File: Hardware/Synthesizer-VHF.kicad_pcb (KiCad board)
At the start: 2 copper layers, 45.8 x 32.5 mm, 81 parts, among them J1 REF Select, J2 REF_IN, J3 RFOUTA, J4 RFOUTB, J5 USB-C 2.0 16P, J7 Header 1x3, J8 Screw_Terminal_01x12, U10 ADF4350, U2 MC78L05_TO-252, U4 GM1207ACPZ-3.3, U7 GM1207ACPZ-3.3, U8 ATtiny1616-M, U9 FT231XQ, X1 IQXO-70

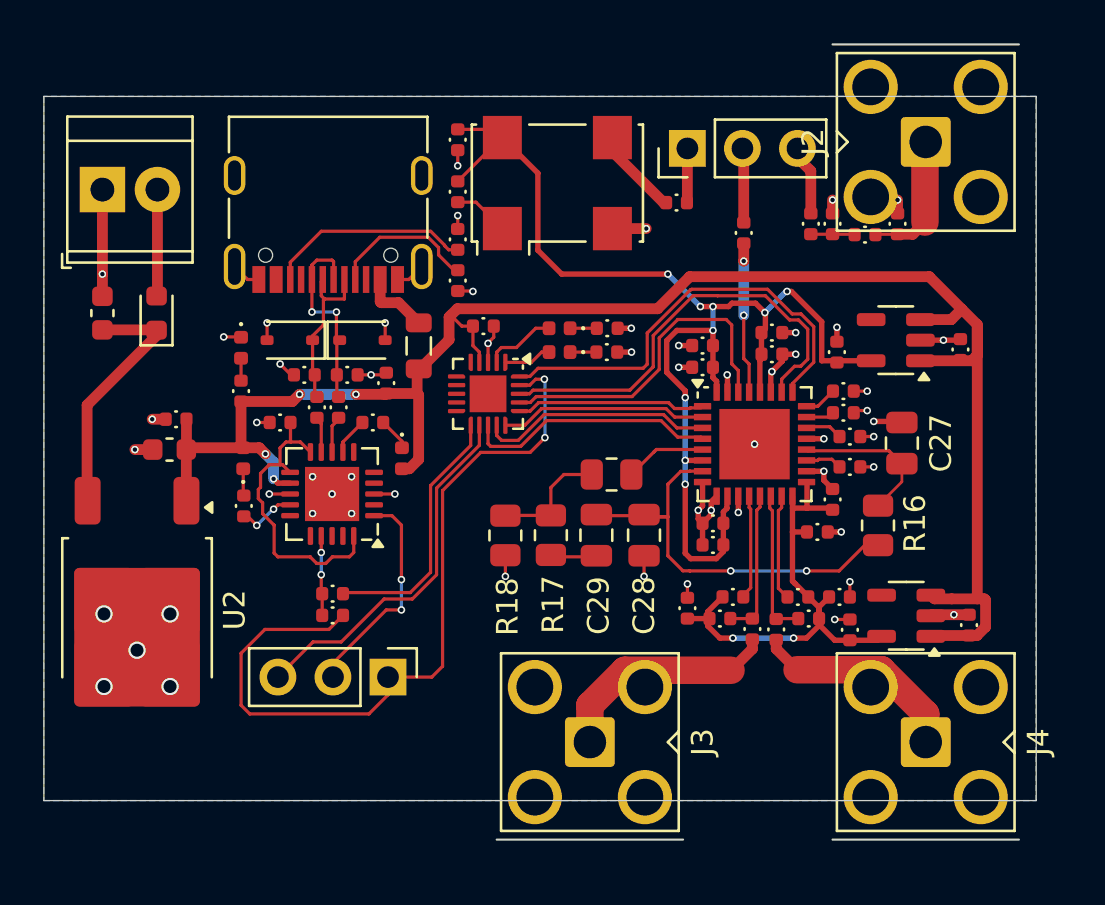
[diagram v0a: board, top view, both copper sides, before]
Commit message: Added test points for scope probes, tweaked layout a bit
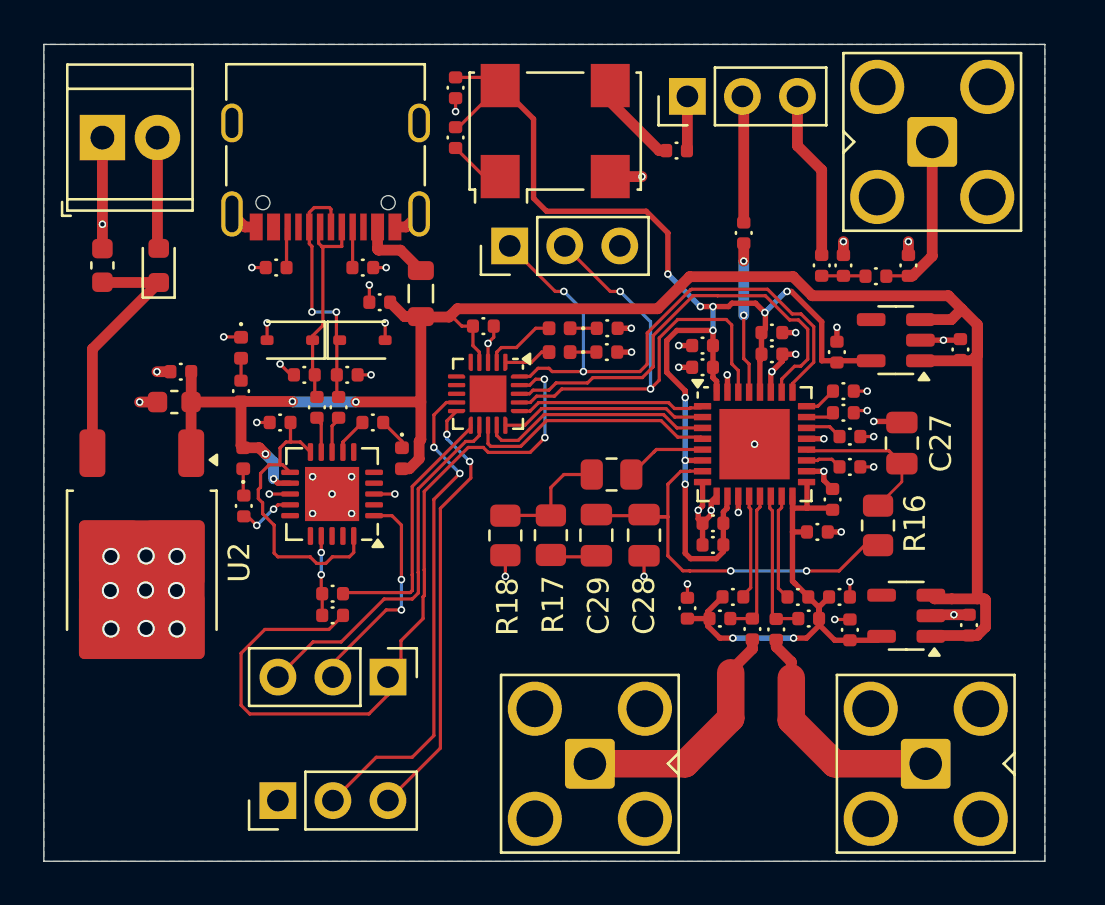
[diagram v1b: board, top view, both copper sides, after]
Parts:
- added J6: Header 1x3, Connector_PinHeader_2.54mm:PinHeader_1x03_P2.54mm_Vertical, F.Cu at (148.8, 85.3)
- added J9: Header 1x3, Connector_PinHeader_2.54mm:PinHeader_1x03_P2.54mm_Vertical, F.Cu at (138.1, 110.9)
- D5: value White -> PA2
- D8: value White -> PA3
- J2, J3, J4: footprint Connector_Coaxial:SMA_Amphenol_901-143_Horizontal -> Synthesizer:SMA_Amphenol_901-143_Horizontal
- moved R10 8.48 mm to (138.0, 86.3), turned to 0 degrees
- moved R7 4.42 mm to (142.0, 86.3), turned to 180 degrees
- moved C44 3.74 mm to (142.8, 87.9), turned to 180 degrees
- moved R21 2.50 mm to (146.3, 80.3)
- moved J5 2.43 mm to (140.3, 80.7)
- moved FB1 2.41 mm to (144.7, 87.5)
- moved C31 2.40 mm to (146.3, 78.0)
- moved X1 2.40 mm to (150.9, 80.0)
- moved J8 2.40 mm to (130.0, 80.3)
- moved J1 2.40 mm to (157.0, 78.4)
- moved R20 2.40 mm to (156.5, 80.9)
- moved C47 2.21 mm to (133.6, 91.1)
- moved C48 2.21 mm to (133.3, 92.5)
- moved U2 2.21 mm to (131.8, 99.9)
- moved D1 2.20 mm to (132.6, 86.2)
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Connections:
- U8 pad 10: unconnected-(U8-PB4-Pad10) -> Net-(J9-Pin_3)
- U8 pad 9: unconnected-(U8-PB5-Pad9) -> Net-(J9-Pin_2)
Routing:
- net Net-(J9-Pin_2): track 0.00 -> 23.0 mm, vias 0 -> 2
- net Net-(J9-Pin_3): track 0.00 -> 20.2 mm, vias 0 -> 2
- net /MUX: track 15.6 -> 24.4 mm, vias 0 -> 2
- net Net-(J5-CC2): track 9.49 -> 1.90 mm
- net /LD: track 20.3 -> 27.9 mm, vias 0 -> 2
- net Net-(J5-CC1): track 6.85 -> 1.88 mm
- net Net-(J1-Pin_3): track 3.25 -> 7.78 mm
- net /VCC_DIG: track 56.0 -> 59.2 mm
- net Net-(D2-K): track 9.39 -> 11.9 mm
- net Net-(D4-K): track 7.69 -> 10.1 mm
- net Net-(J1-Pin_2): track 3.45 -> 5.85 mm
- net /5V: track 82.3 -> 84.5 mm
- net Net-(J2-In): track 6.24 -> 7.77 mm
- net Net-(J4-In): track 9.86 -> 11.0 mm
- net Net-(J3-In): track 10.7 -> 11.4 mm
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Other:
- board size 45.8 x 32.5 mm -> 46.2 x 37.7 mm

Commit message: Tried to find a better TCXO at 40 MHz, but jlcpcb froze all of kicad several times.
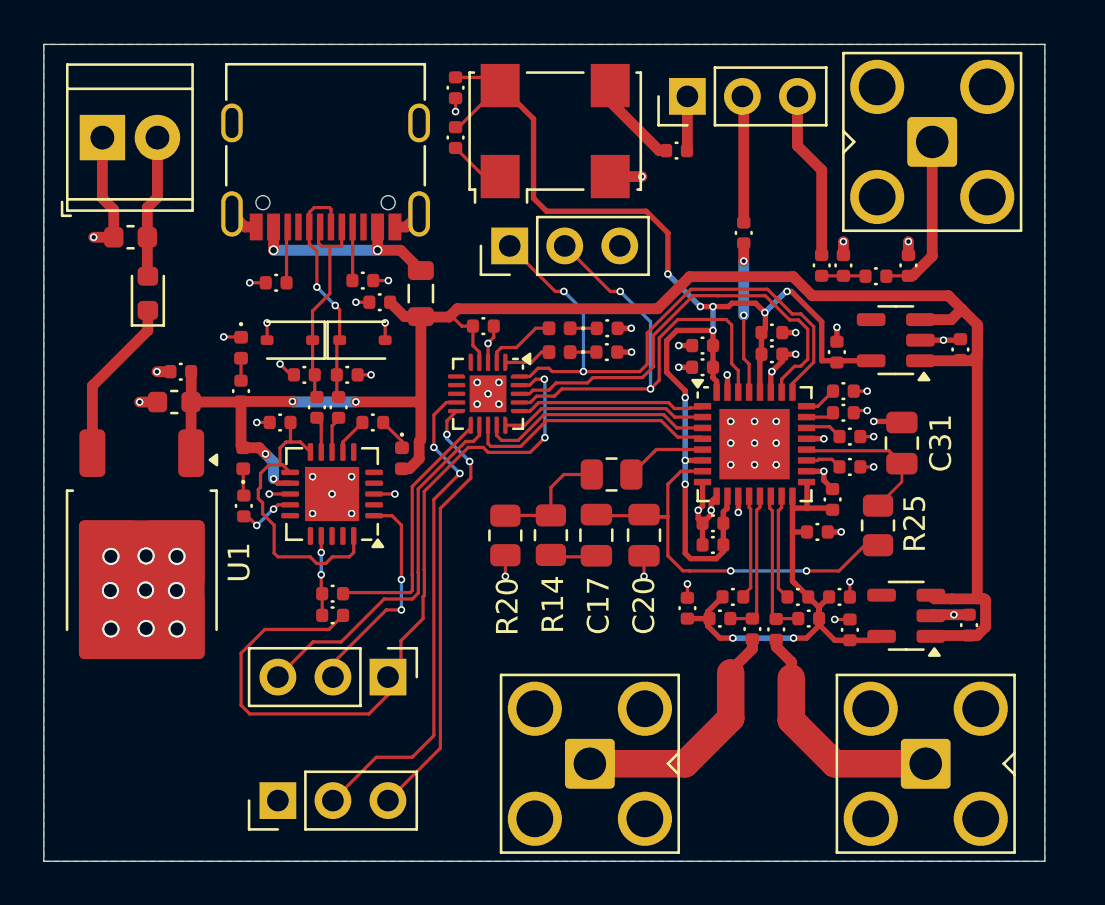
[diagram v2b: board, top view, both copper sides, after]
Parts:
- moved C1 1.84 mm to (131.3, 84.9), turned to 180 degrees
- moved D1 1.38 mm to (132.1, 87.5)
- moved R1 0.70 mm to (138.0, 87.0)
- moved R3 0.60 mm to (142.0, 86.9)
- renumbered C26 to C1, C5 to C10, C45 to C11, C6 to C12, C11 to C13, C34 to C14, C1 to C15, C2 to C16, C29 to C17, C9 to C18, C12 to C19, C44 to C2, C28 to C20, C8 to C21, C24 to C22, C22 to C23, C16 to C24, C15 to C25, C4 to C26, C41 to C27, C10 to C28, C42 to C29, C7 to C30, C27 to C31, C40 to C32, C35 to C33, C13 to C4, C31 to C5, C47 to C6, C46 to C7, C48 to C8, C43 to C9, D4 to D2, D6 to D4, D7 to D5, D2 to D6, D5 to D7, J8 to J1, J6 to J2, J1 to J3, J5 to J4, J2 to J5, J9 to J6, J3 to J7, J7 to J8, J4 to J9, R10 to R1, R26 to R10, R6 to R11, R30 to R12, R25 to R13, R17 to R14, R5 to R15, R29 to R16, R12 to R17, R8 to R18, R28 to R19, R20 to R2, R18 to R20, R3 to R21, R4 to R22, R2 to R23, R16 to R25, R7 to R3, R21 to R4, R9 to R5, R19 to R6, R1 to R7, R27 to R8, R11 to R9, U2 to U1, U9 to U2, U8 to U3, U10 to U4, U7 to U5, U4 to U6
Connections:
- C1 pad 1: Net-(D1-K) -> /12V
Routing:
- net Net-(FB1-Pad1): track 3.43 -> 9.34 mm, vias 0 -> 2
- net Net-(D1-K): track 11.8 -> 7.69 mm
- net /12V: track 5.14 -> 6.60 mm
- net Net-(J5-CC2): track 1.90 -> 2.60 mm
- net Net-(D2-K): track 11.9 -> 11.2 mm
- net GND: track 50.0 -> 50.7 mm, vias 61 -> 74
- net Net-(J5-CC1): track 1.88 -> 2.48 mm

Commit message: Complete design used for pricing experient.   0.2 mm drilled vias cost a lot.   had assembling through hole adds a lot   4 layers is is free Next up,   climb the learning curve on 4 layer design   price components on both sides
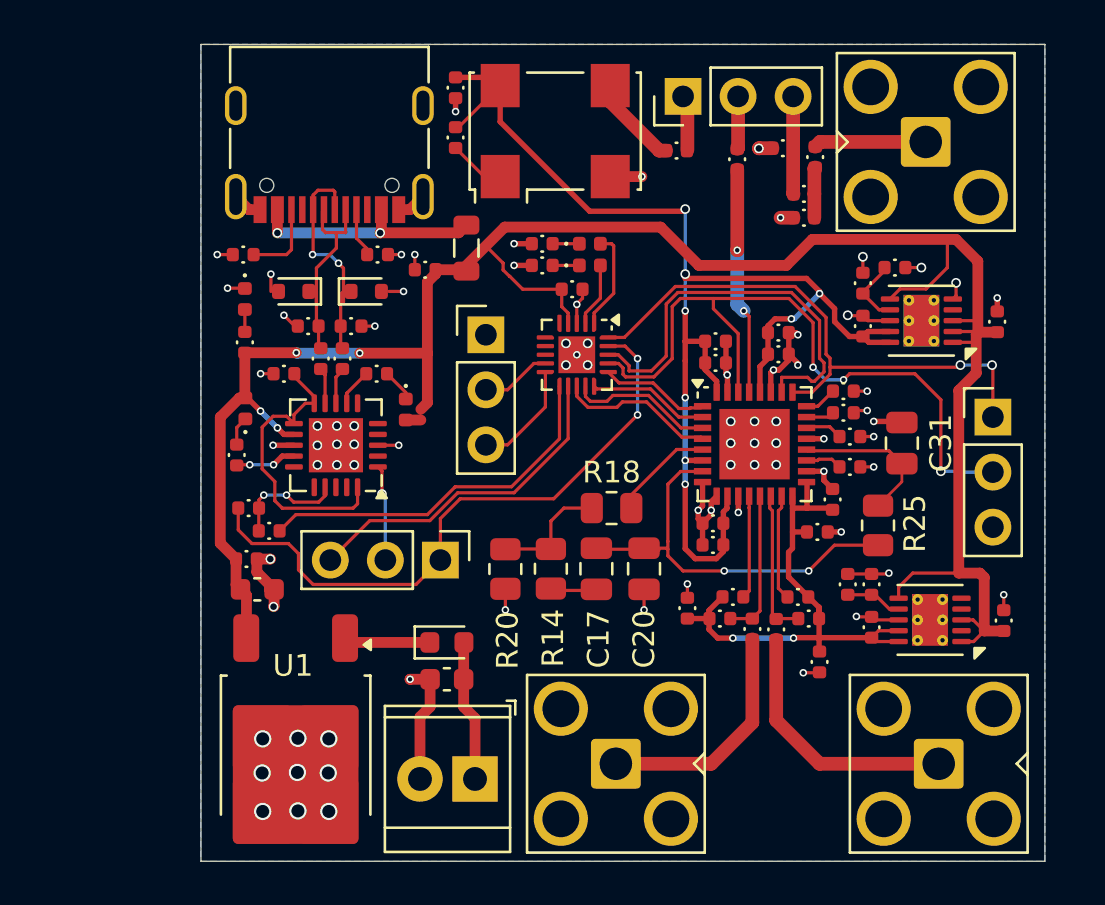
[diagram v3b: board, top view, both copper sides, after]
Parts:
- added C34: 4.7u 10V, Synthesizer:Cap_0402, F.Cu at (165.1, 87.0)
- added C35: 4.7u 10V, Synthesizer:Cap_0402, F.Cu at (165.5, 100.9)
- added R26: 33K2, Synthesizer:Res_0402, F.Cu at (164.4, 100.9)
- added R27: 33K2, Synthesizer:Res_0402, F.Cu at (166.6, 86.3)
- C1: value 330n 25V -> 330n 50V
- C14, C27, C32, C33: value 2.2u -> 4.7u 10V
- C2, C29, C6, C7: value .1u -> 100n
- C31: value 680 -> 680p
- D2, D6: footprint Diode_SMD:D_SOD-323 -> Diode_SMD:D_SOD-523
- J1: value Screw_Terminal_01x12 -> Screw_Terminal_01x02
- J2, J6: value Header 1x3 -> Scope
- R13, R24: value 22 -> 22R
- R2: value 0 -> 0R
- U1: value MC78L05_TO-252 -> LM7805A
- U5, U6: value GM1207ACPZ-3.3 -> GM1200ACPZ; footprint Package_TO_SOT_SMD:SOT-23-5 -> Package_DFN_QFN:DFN-10-1EP_3x3mm_P0.5mm_EP1.65x2.38mm_ThermalVias
- moved J1 34.2 mm to (147.2, 109.9), turned to 180 degrees
- moved C1 25.1 mm to (145.9, 105.3)
- moved J2 23.7 mm to (171.1, 93.2), turned to 0 degrees
- moved J6 23.5 mm to (147.7, 89.4), turned to 0 degrees
- moved D1 21.2 mm to (145.9, 103.6), turned to 0 degrees
- moved U1 11.1 mm to (138.9, 108.4)
- moved C8 9.45 mm to (137.2, 101.2), turned to 0 degrees
- moved C6 9.16 mm to (136.7, 99.8), turned to 0 degrees
- moved R6 7.93 mm to (161.4, 80.8), turned to 180 degrees
- moved R12 6.29 mm to (136.8, 97.4), turned to 180 degrees
- moved J8 5.92 mm to (145.6, 99.8)
- moved R10 5.82 mm to (150.3, 85.2), turned to 180 degrees
- moved D7 5.19 mm to (152.5, 85.2), turned to 0 degrees
- moved R7 5.05 mm to (162.4, 82.9)
- moved C4 5.01 mm to (162.9, 81.2), turned to 90 degrees
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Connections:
- C4 pad 1: Net-(J1-Pin_3) -> Net-(C4-Pad1)
- C4 pad 2: Net-(C13-Pad2) -> Net-(J5-In)
- J1 pad 1: GND -> /12V
- J1 pad 2: /12V -> GND
- J3 pad 3: Net-(J1-Pin_3) -> Net-(J3-Pin_3)
- J5 pad 1: Net-(J2-In) -> Net-(J5-In)
- R5 pad 1: Net-(C13-Pad2) -> Net-(C4-Pad1)
- R6 pad 1: Net-(J2-In) -> Net-(J3-Pin_3)
- R7 pad 1: Net-(J2-In) -> Net-(C4-Pad1)
- R7 pad 2: Net-(C13-Pad2) -> Net-(J3-Pin_3)
- U1 pad 1: /5V -> Net-(D1-K)
- U1 pad 3: Net-(D1-K) -> /5V
- U2 pad 19: /RTS\ -> unconnected-(U2-~{RTS}-Pad19)
- U2 pad 6: /CTS\ -> unconnected-(U2-~{CTS}-Pad6)
- U5 pad 2: GND -> /5V
- U5 pad 5: /VCC_DIG -> GND
- U6 pad 2: GND -> /5V
- U6 pad 5: /VCC_RF -> GND
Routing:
- net Net-(J6-Pin_2): track 23.0 -> 3.25 mm, vias 2 -> 0
- net /5V: track 84.5 -> 100.9 mm
- net Net-(J6-Pin_3): track 20.2 -> 5.08 mm, vias 2 -> 0
- net /MUX: track 24.4 -> 32.6 mm, vias 2 -> 3
- net GND: track 50.7 -> 58.8 mm, vias 74 -> 80
- net Net-(J1-Pin_3): track 7.78 -> 0.00 mm
- net Net-(J2-In): track 7.77 -> 0.00 mm
- net /UPDI: track 35.9 -> 29.5 mm
- net /RXD_U: track 10.2 -> 4.44 mm, vias 2 -> 1
- net Net-(J5-In): track 0.00 -> 5.49 mm
- net /RXD_M: track 12.0 -> 17.1 mm
- net Net-(J3-Pin_3): track 0.00 -> 4.51 mm
- net /CE: track 11.6 -> 7.29 mm
- net /LE: track 10.8 -> 6.71 mm
- net /DATA: track 9.58 -> 5.60 mm
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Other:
- board size 46.2 x 37.7 mm -> 38.9 x 37.7 mm

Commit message: Updated layout for 4 layer board as an experiment to check costs Changed low noise regulators to ADP150...used in the Eval board and fancy sig gen example Add more analysis to phase noise spreadsheet, apparently the low V/Hz of the VCO allows cheap regulators
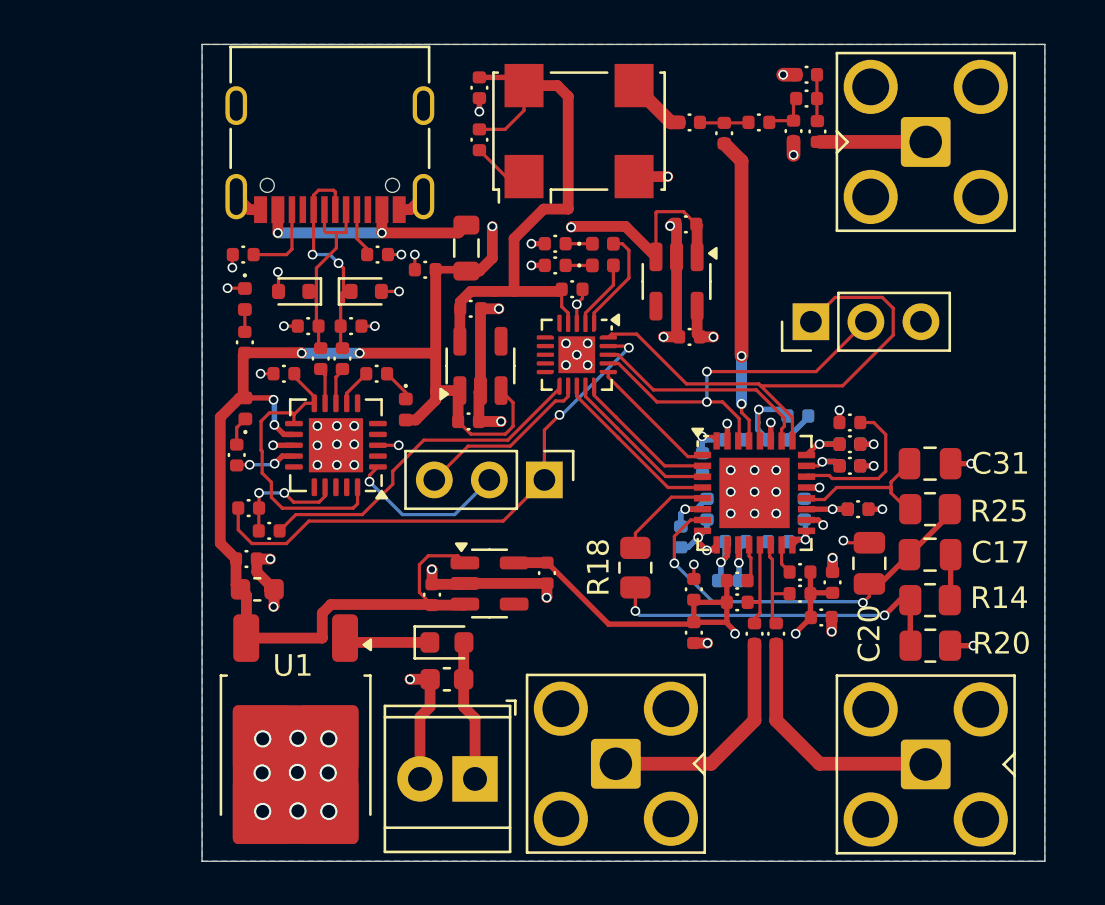
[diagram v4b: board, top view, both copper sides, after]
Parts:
- removed C34, C35: 4.7u 10V, Synthesizer:Cap_0402
- removed J3: REF Select, Connector_PinHeader_2.54mm:PinHeader_1x03_P2.54mm_Vertical
- removed J6: Scope, Connector_PinHeader_2.54mm:PinHeader_1x03_P2.54mm_Vertical
- removed R26, R27: 33K2, Synthesizer:Res_0402
- added C36: 10p, Synthesizer:Cap_0402, B.Cu at (164.5, 94.5)
- added C37: 10p, Synthesizer:Cap_0402, B.Cu at (164.5, 95.5)
- added C38: 10p, Synthesizer:Cap_0402, B.Cu at (164.9, 97.4)
- added C39: 100n, Synthesizer:Cap_0402, B.Cu at (158.9, 100.8)
- added C40: 10p, Synthesizer:Cap_0402, B.Cu at (159.2, 98.9)
- added C41: 100n, Synthesizer:Cap_0402, F.Cu at (157.3, 103.2)
- added C42: 100n, Synthesizer:Cap_0402, F.Cu at (163.2, 102.4)
- added C43: 120p, Synthesizer:Cap_0402, F.Cu at (163.7, 100.8)
- added C44: 1u, Synthesizer:Cap_0402, F.Cu at (146.9, 93.4)
- added R28: NP, Synthesizer:Res_0402, F.Cu at (160.3, 79.6)
- added U7: ADP150AUJZ-3.3-R7, Package_TO_SOT_SMD:SOT-23-5, F.Cu at (147.4, 90.8)
- C13, C18, C25, C30: value 10n -> 100n; moved to B.Cu
- C14, C27, C32, C33: value 4.7u 10V -> 1u
- C15: value 100n -> 120p
- C19, C21, C24, C28: value 100p -> 10p; moved to B.Cu
- C22: value 100n -> 1u
- C3: value 10n -> 1n
- U4: value ADF4350 -> ADF435x
- U5, U6: value GM1200ACPZ -> ADP150AUJZ-3.3-R7; footprint Package_DFN_QFN:DFN-10-1EP_3x3mm_P0.5mm_EP1.65x2.38mm_ThermalVias -> Package_TO_SOT_SMD:SOT-23-5
- moved C22 22.9 mm to (147.0, 88.2), turned to 0 degrees
- moved C33 21.2 mm to (150.5, 100.4), turned to -90 degrees
- moved U6 20.4 mm to (147.9, 100.9), turned to 0 degrees
- moved C14 20.3 mm to (145.2, 101.4)
- moved R20 19.9 mm to (168.2, 103.8), turned to 0 degrees
- moved R14 17.6 mm to (168.2, 101.7), turned to 180 degrees
- moved C17 15.4 mm to (168.2, 99.5), turned to 0 degrees
- moved C32 14.2 mm to (157.1, 89.5), turned to 180 degrees
- moved U5 11.4 mm to (156.5, 86.9), turned to -90 degrees
- moved C20 10.4 mm to (165.4, 100.0), turned to 90 degrees
- moved J2 9.48 mm to (162.7, 88.8), turned to 90 degrees
- moved C27 9.42 mm to (156.9, 84.3), turned to 180 degrees
- moved R5 6.60 mm to (162.5, 77.4)
- moved J8 6.06 mm to (150.4, 96.1)
- moved C13 5.68 mm to (157.7, 95.3), turned to -90 degrees
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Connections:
- C13 pad 1: /VCC_DIG -> /VCC_1
- C14 pad 1: /VCC_RF -> /5V
- C15 pad 1: /VCC_RF -> /VCC_2
- C18 pad 1: /VCC_RF -> /VCC_1
- C19 pad 2: /VCC_DIG -> /VCC_1
- C21 pad 2: /VCC_DIG -> /VCC_1
- C22 pad 1: /VCC_RF -> /3V3_MCU
- C24 pad 1: /VCC_DIG -> /VCC_1
- C25 pad 1: /VCC_DIG -> /VCC_1
- C27 pad 1: /VCC_DIG -> /5V
- C28 pad 2: /VCC_RF -> /VCC_1
- C29 pad 1: /5V -> /3V3_MCU
- C3 pad 2: Net-(J3-Pin_2) -> Net-(C3-Pad2)
- C30 pad 1: /VCC_DIG -> /VCC_1
- C32 pad 1: /5V -> /VCC_1
- C33 pad 1: /5V -> /VCC_2
- C5 pad 2: /VCC_DIG -> /3V3_MCU
- R11 pad 2: /VCC_RF -> /VCC_2
- R15 pad 2: /VCC_RF -> /VCC_2
- R2 pad 1: Net-(X1-OUT) -> Net-(C3-Pad2)
- R2 pad 2: Net-(J3-Pin_1) -> Net-(X1-OUT)
- R21 pad 2: /VCC_RF -> /VCC_2
- R23 pad 2: /VCC_RF -> /VCC_2
- R4 pad 2: /VCC_DIG -> /3V3_MCU
- U3 pad 10: Net-(J6-Pin_3) -> unconnected-(U3-PB4-Pad10)
- U3 pad 4: /5V -> /3V3_MCU
- U3 pad 9: Net-(J6-Pin_2) -> unconnected-(U3-PB5-Pad9)
- U4 pad 10: /VCC_DIG -> /VCC_1
- U4 pad 16: /VCC_RF -> /VCC_1
- U4 pad 17: /VCC_RF -> /VCC_1
- U4 pad 28: /VCC_DIG -> /VCC_1
- U4 pad 32: /VCC_DIG -> /VCC_1
- U4 pad 6: /VCC_DIG -> /VCC_1
- U5 pad 2: /5V -> GND
- U5 pad 5: GND -> /VCC_1
- U6 pad 2: /5V -> GND
- U6 pad 5: GND -> /VCC_2
- X1 pad 4: /VCC_DIG -> /3V3_MCU
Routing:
- net /VCC_DIG: track 61.3 -> 0.00 mm, vias 8 -> 0
- net /3V3_MCU: track 0.00 -> 27.2 mm
- net /VCC_RF: track 25.3 -> 0.00 mm, vias 2 -> 0
- net /5V: track 100.9 -> 76.2 mm, vias 4 -> 6
- net /VCC_2: track 0.00 -> 23.2 mm, vias 0 -> 2
- net /VCC_1: track 0.00 -> 18.0 mm, vias 0 -> 6
- net /MUX: track 32.6 -> 17.8 mm, vias 3 -> 2
- net Net-(R14-Pad2): track 5.51 -> 16.3 mm, vias 0 -> 2
- net /RF_EN: track 19.0 -> 10.4 mm
- net /TXD_M: track 15.7 -> 8.25 mm
- net GND: track 58.8 -> 66.3 mm, vias 80 -> 77
- net Net-(U4-RSET): track 1.73 -> 7.08 mm
- net Net-(J6-Pin_3): track 5.08 -> 0.00 mm
- net /UPDI: track 29.5 -> 25.4 mm
- net Net-(U4-REFIN): track 10.5 -> 14.2 mm
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- added copper zone on In2.Cu, net /VCC_1
- added copper zone on In1.Cu, net GND
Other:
- copper layers 2 -> 4
